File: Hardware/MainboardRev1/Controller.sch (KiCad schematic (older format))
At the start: 15 parts, among them Q22 NTR4003, Q23 NTR4003, Q24 NTR4003, U11 Teensy3.6

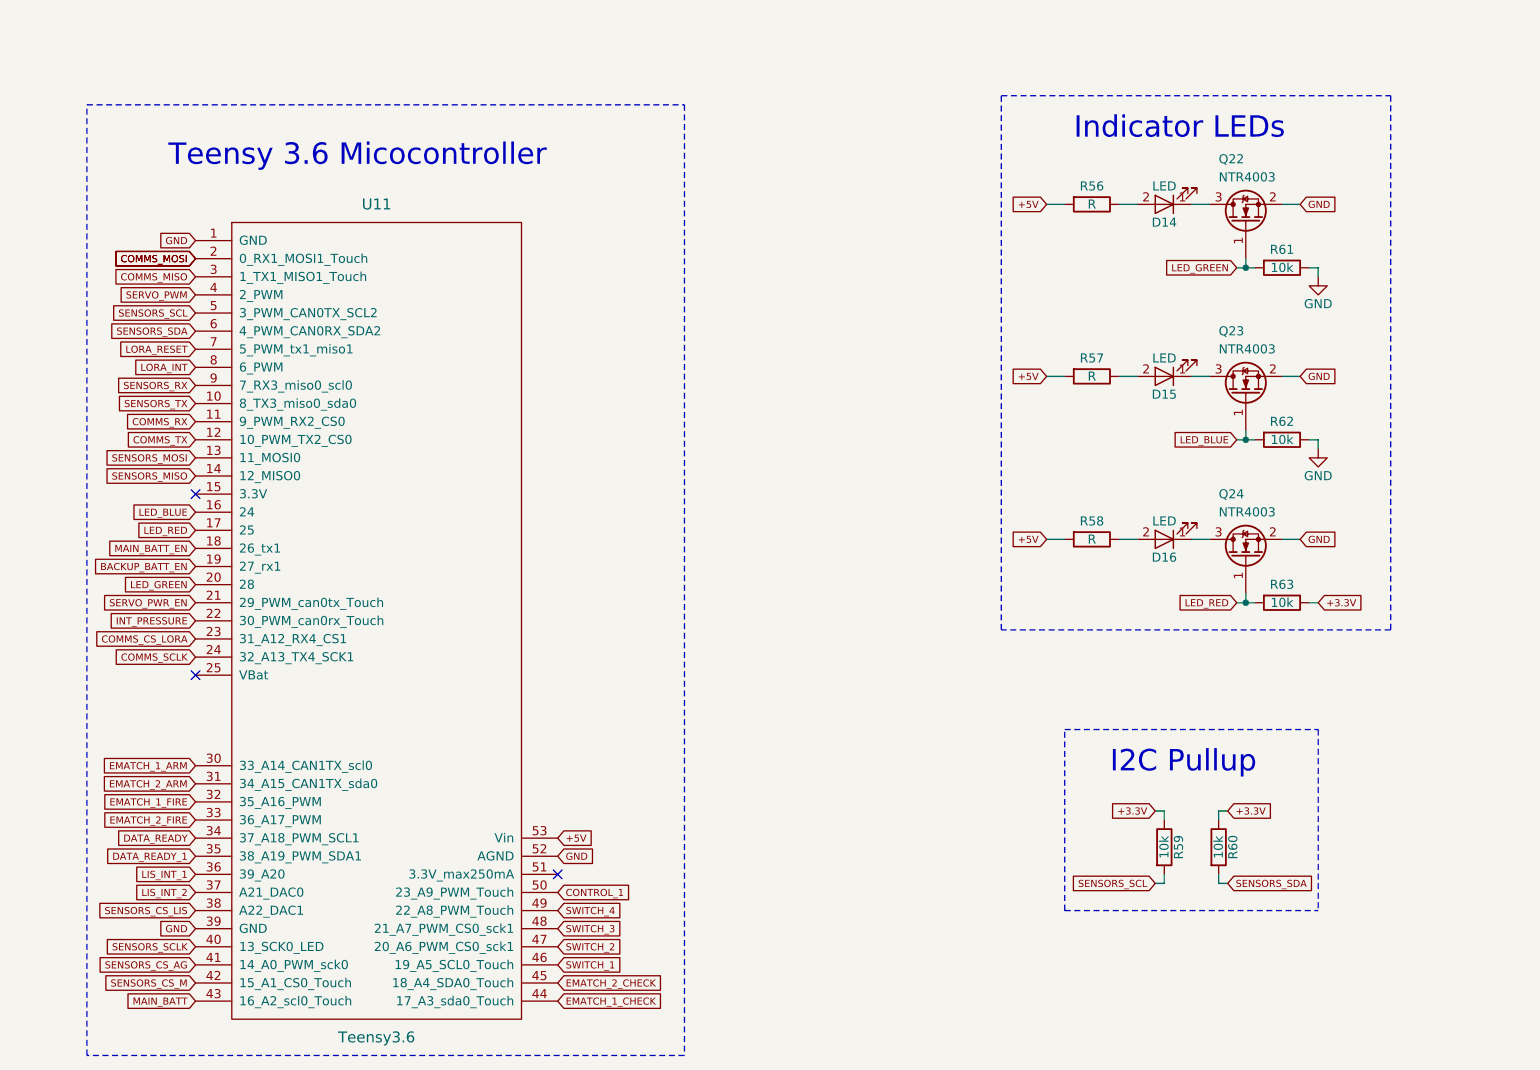
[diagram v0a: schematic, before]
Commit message: Small changes to schematic: Added voltage dividers for analog inputs, small net changes. Added footprints for each part
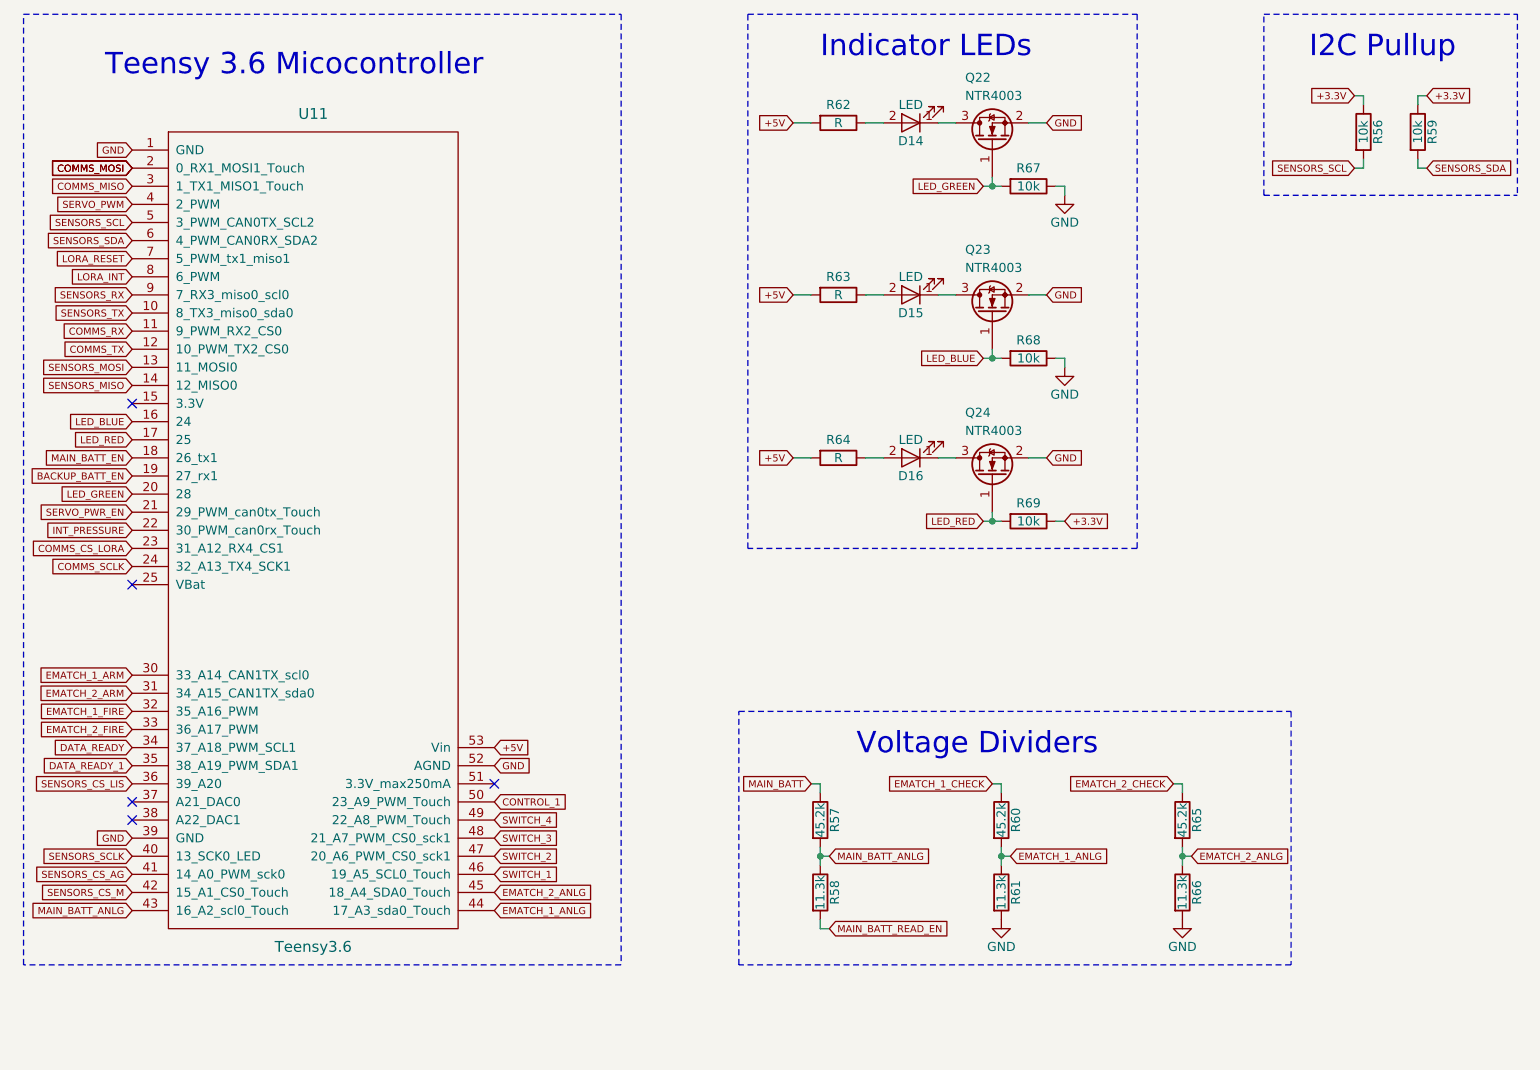
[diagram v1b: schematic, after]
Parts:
- added R57, R60, R65: 45.2k, Resistors_SMD:R_0603_HandSoldering, symbol R
- added R58, R61, R66: 11.3k, Resistors_SMD:R_0603_HandSoldering, symbol R
- D14, D15, D16: footprint (none) -> LEDs:LED_0603_HandSoldering
- Q22, Q23, Q24: footprint (none) -> TO_SOT_Packages_SMD:SOT-23
- R56: renamed from R59; footprint (none) -> Resistors_SMD:R_0603_HandSoldering
- R59: renamed from R60; footprint (none) -> Resistors_SMD:R_0603_HandSoldering
- R62: renamed from R56; footprint (none) -> Resistors_SMD:R_0603_HandSoldering
- R63: renamed from R57; footprint (none) -> Resistors_SMD:R_0603_HandSoldering
- R64: renamed from R58; footprint (none) -> Resistors_SMD:R_0603_HandSoldering
- R67: renamed from R61; footprint (none) -> Resistors_SMD:R_0603_HandSoldering
- R68: renamed from R62; footprint (none) -> Resistors_SMD:R_0603_HandSoldering
- R69: renamed from R63; footprint (none) -> Resistors_SMD:R_0603_HandSoldering
- U11: footprint (none) -> Dans_Parts:Teensy33_SidePinsAndVBatt
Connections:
- net LIS_INT_1 is gone; now on net SENSORS_CS_LIS: U11.36 (39_A20)
- net EMATCH_1_CHECK: now also R60.1; no longer U11.44 (17_A3_sda0_Touch)
- net EMATCH_2_CHECK: now also R65.1; no longer U11.45 (18_A4_SDA0_Touch)
- net GND: now also R61.2, R66.2
- net MAIN_BATT: now also R57.1; no longer U11.43 (16_A2_scl0_Touch)
- net SENSORS_CS_LIS: no longer U11.38 (A22_DAC1)
- net LIS_INT_2: no longer names the net of U11.37 (A21_DAC0)
- new net EMATCH_1_ANLG: R60.2, R61.1, U11.44 (17_A3_sda0_Touch)
- new net EMATCH_2_ANLG: R65.2, R66.1, U11.45 (18_A4_SDA0_Touch)
- new net MAIN_BATT_ANLG: R57.2, R58.1, U11.43 (16_A2_scl0_Touch)
- new net MAIN_BATT_READ_EN: R58.2
- no-connect marks 3 -> 5
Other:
- note added: "Voltage Dividers"
- moved on the sheet: D14, D15, D16, Q22, Q23, Q24, R56, R59, R62, R63, R64, R67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

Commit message: Components placed. Needs to be routed.
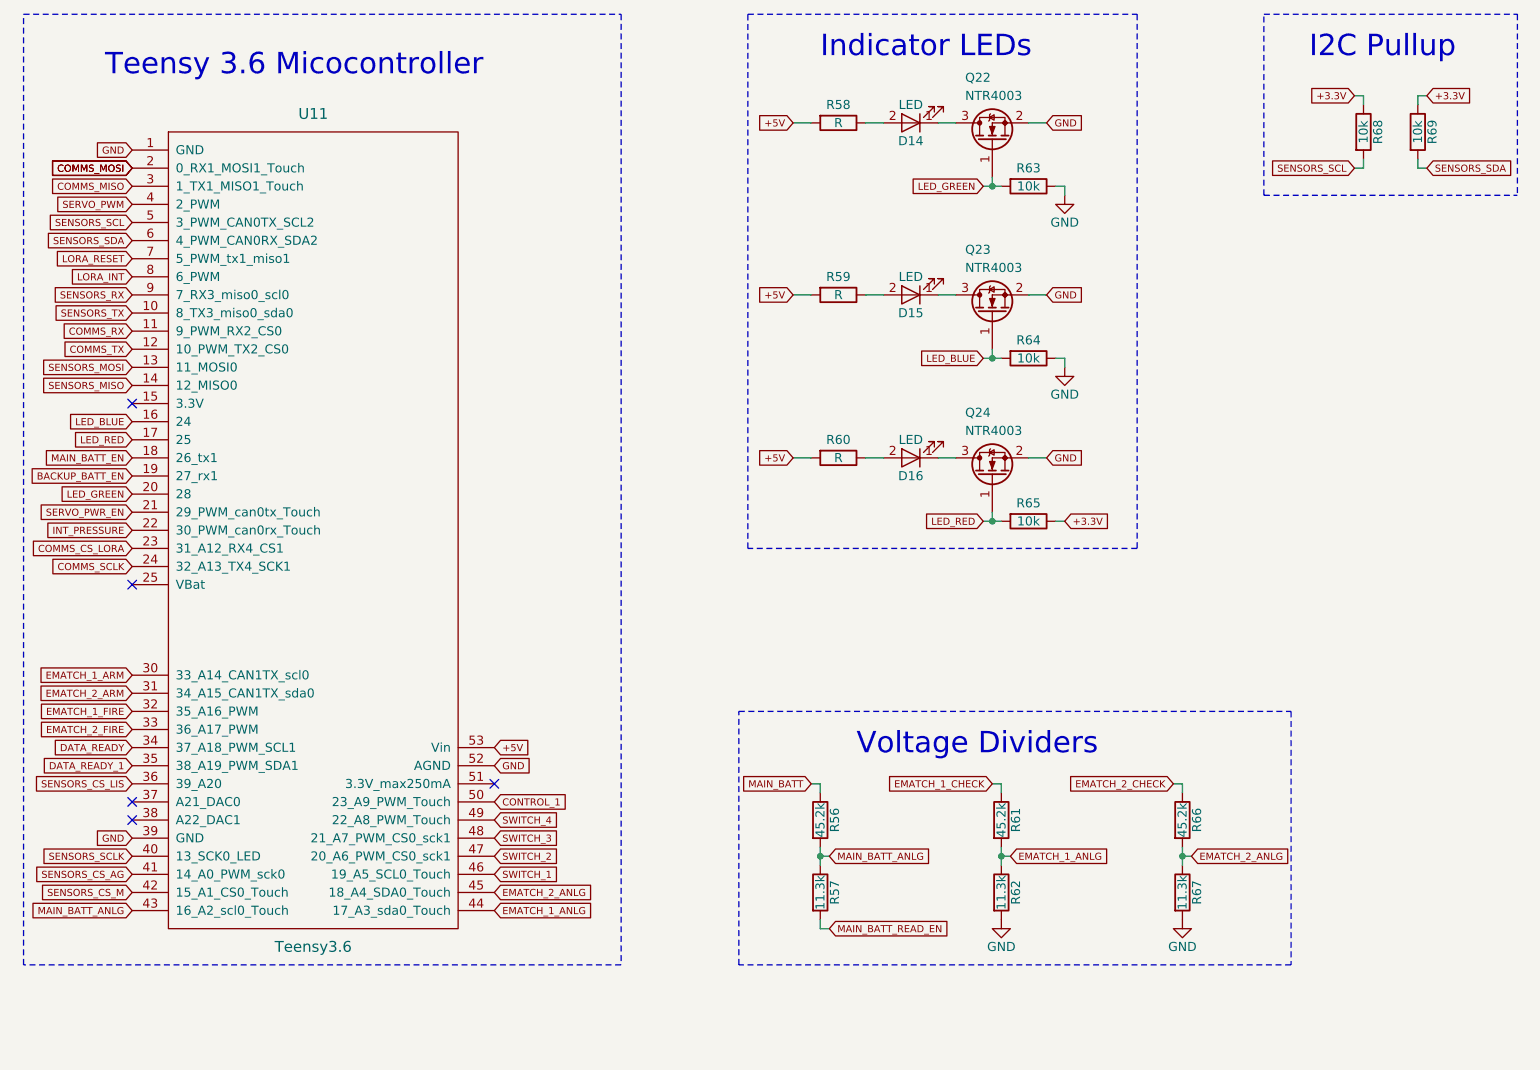
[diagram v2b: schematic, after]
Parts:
- renumbered R57 to R56, R58 to R57, R62 to R58, R63 to R59, R64 to R60, R60 to R61, R61 to R62, R67 to R63, R68 to R64, R69 to R65, R65 to R66, R66 to R67, R56 to R68, R59 to R69
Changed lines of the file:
@@
 LIBS:teensy3_6-OuterHeadersOnly
 LIBS:switches
+LIBS:mounting_hole_eighth_inch
 LIBS:MainboardRev1-cache
 EELAYER 25 0
@@
 GND
 $Comp
-L R R62
+L R R58
 U 1 1 5AFD53B2
 P 6050 1450
-F 0 "R62" V 5950 1450 50  0000 C CNN
+F 0 "R58" V 5950 1450 50  0000 C CNN
 F 1 "R" V 6050 1450 50  0000 C CNN
 F 2 "Resistors_SMD:R_0603_HandSoldering" V 5980 1450 50  0001 C CNN
@@
 LED_GREEN
 $Comp
-L R R67
+L R R63
 U 1 1 5AFD592A
 P 7100 1800
-F 0 "R67" V 7000 1800 50  0000 C CNN
+F 0 "R63" V 7000 1800 50  0000 C CNN
 F 1 "10k" V 7100 1800 50  0000 C CNN
 F 2 "Resistors_SMD:R_0603_HandSoldering" V 7030 1800 50  0001 C CNN
@@
 Connection ~ 6900 1800
 $Comp
-L GND #PWR046
+L GND #PWR052
 U 1 1 5AFD5996
 P 7300 1850
-F 0 "#PWR046" H 7300 1600 50  0001 C CNN
+F 0 "#PWR052" H 7300 1600 50  0001 C CNN
 F 1 "GND" H 7300 1700 50  0000 C CNN
 F 2 "" H 7300 1850 50  0001 C CNN
@@
 GND
 $Comp
-L R R63
+L R R59
 U 1 1 5AFD5AC4
 P 6050 2400
-F 0 "R63" V 5950 2400 50  0000 C CNN
+F 0 "R59" V 5950 2400 50  0000 C CNN
 F 1 "R" V 6050 2400 50  0000 C CNN
 F 2 "Resistors_SMD:R_0603_HandSoldering" V 5980 2400 50  0001 C CNN
@@
 LED_BLUE
 $Comp
-L R R68
+L R R64
 U 1 1 5AFD5ACF
 P 7100 2750
-F 0 "R68" V 7000 2750 50  0000 C CNN
+F 0 "R64" V 7000 2750 50  0000 C CNN
 F 1 "10k" V 7100 2750 50  0000 C CNN
 F 2 "Resistors_SMD:R_0603_HandSoldering" V 7030 2750 50  0001 C CNN
@@
 Connection ~ 6900 2750
 $Comp
-L GND #PWR047
+L GND #PWR053
 U 1 1 5AFD5AD8
 P 7300 2800
-F 0 "#PWR047" H 7300 2550 50  0001 C CNN
+F 0 "#PWR053" H 7300 2550 50  0001 C CNN
 F 1 "GND" H 7300 2650 50  0000 C CNN
 F 2 "" H 7300 2800 50  0001 C CNN
@@
 GND
 $Comp
-L R R64
+L R R60
 U 1 1 5AFD5BE7
 P 6050 3300
-F 0 "R64" V 5950 3300 50  0000 C CNN
+F 0 "R60" V 5950 3300 50  0000 C CNN
 F 1 "R" V 6050 3300 50  0000 C CNN
 F 2 "Resistors_SMD:R_0603_HandSoldering" V 5980 3300 50  0001 C CNN
@@
 LED_RED
 $Comp
-L R R69
+L R R65
 U 1 1 5AFD5BF2
 P 7100 3650
-F 0 "R69" V 7000 3650 50  0000 C CNN
+F 0 "R65" V 7000 3650 50  0000 C CNN
 F 1 "10k" V 7100 3650 50  0000 C CNN
 F 2 "Resistors_SMD:R_0603_HandSoldering" V 7030 3650 50  0001 C CNN
@@
 	8950 1700 8950 1650
 $Comp
-L R R56
+L R R68
 U 1 1 5AFD610C
 P 8950 1500
-F 0 "R56" V 9030 1500 50  0000 C CNN
+F 0 "R68" V 9030 1500 50  0000 C CNN
 F 1 "10k" V 8950 1500 50  0000 C CNN
 F 2 "Resistors_SMD:R_0603_HandSoldering" V 8880 1500 50  0001 C CNN
@@
 	8950 1300 8950 1350
 $Comp
-L R R59
+L R R69
 U 1 1 5AFD61B1
 P 9250 1500
-F 0 "R59" V 9330 1500 50  0000 C CNN
+F 0 "R69" V 9330 1500 50  0000 C CNN
 F 1 "10k" V 9250 1500 50  0000 C CNN
 F 2 "Resistors_SMD:R_0603_HandSoldering" V 9180 1500 50  0001 C CNN
@@
 Voltage Dividers
 $Comp
-L R R57
+L R R56
 U 1 1 5AFCDCCB
 P 5950 5300
-F 0 "R57" V 6030 5300 50  0000 C CNN
+F 0 "R56" V 6030 5300 50  0000 C CNN
 F 1 "45.2k" V 5950 5300 50  0000 C CNN
 F 2 "Resistors_SMD:R_0603_HandSoldering" V 5880 5300 50  0001 C CNN
@@
 $EndComp
 $Comp
-L R R58
+L R R57
 U 1 1 5AFCDD5E
 P 5950 5700
-F 0 "R58" V 6030 5700 50  0000 C CNN
+F 0 "R57" V 6030 5700 50  0000 C CNN
 F 1 "11.3k" V 5950 5700 50  0000 C CNN
 F 2 "Resistors_SMD:R_0603_HandSoldering" V 5880 5700 50  0001 C CNN
@@
 EMATCH_1_CHECK
 $Comp
-L R R60
+L R R61
 U 1 1 5AFD293E
 P 6950 5300
-F 0 "R60" V 7030 5300 50  0000 C CNN
+F 0 "R61" V 7030 5300 50  0000 C CNN
 F 1 "45.2k" V 6950 5300 50  0000 C CNN
 F 2 "Resistors_SMD:R_0603_HandSoldering" V 6880 5300 50  0001 C CNN
@@
 $EndComp
 $Comp
-L R R61
+L R R62
 U 1 1 5AFD2944
 P 6950 5700
-F 0 "R61" V 7030 5700 50  0000 C CNN
+F 0 "R62" V 7030 5700 50  0000 C CNN
 F 1 "11.3k" V 6950 5700 50  0000 C CNN
 F 2 "Resistors_SMD:R_0603_HandSoldering" V 6880 5700 50  0001 C CNN
@@
 Connection ~ 6950 5500
 $Comp
-L GND #PWR048
+L GND #PWR054
 U 1 1 5AFD29A3
 P 6950 5850
-F 0 "#PWR048" H 6950 5600 50  0001 C CNN
+F 0 "#PWR054" H 6950 5600 50  0001 C CNN
 F 1 "GND" H 6950 5700 50  0000 C CNN
 F 2 "" H 6950 5850 50  0001 C CNN
@@
 EMATCH_2_CHECK
 $Comp
-L R R65
+L R R66
 U 1 1 5AFD2CA4
 P 7950 5300
-F 0 "R65" V 8030 5300 50  0000 C CNN
+F 0 "R66" V 8030 5300 50  0000 C CNN
 F 1 "45.2k" V 7950 5300 50  0000 C CNN
 F 2 "Resistors_SMD:R_0603_HandSoldering" V 7880 5300 50  0001 C CNN
@@
 $EndComp
 $Comp
-L R R66
+L R R67
 U 1 1 5AFD2CAA
 P 7950 5700
-F 0 "R66" V 8030 5700 50  0000 C CNN
+F 0 "R67" V 8030 5700 50  0000 C CNN
 F 1 "11.3k" V 7950 5700 50  0000 C CNN
 F 2 "Resistors_SMD:R_0603_HandSoldering" V 7880 5700 50  0001 C CNN
@@
 Connection ~ 7950 5500
 $Comp
-L GND #PWR049
+L GND #PWR055
 U 1 1 5AFD2CB6
 P 7950 5850
-F 0 "#PWR049" H 7950 5600 50  0001 C CNN
+F 0 "#PWR055" H 7950 5600 50  0001 C CNN
 F 1 "GND" H 7950 5700 50  0000 C CNN
 F 2 "" H 7950 5850 50  0001 C CNN
